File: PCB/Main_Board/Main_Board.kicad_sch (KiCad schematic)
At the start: 34 parts, among them J1 POWER_SUPPLY, J2 LIMIT_SWITCH, J3 ToF, J4 BUCK_IN, J5 BUCK_OUT, J6 ESP32_Left, J7 ESP32_Right, J8 CABLE, J9 MOTOR, U1 74AHCT125

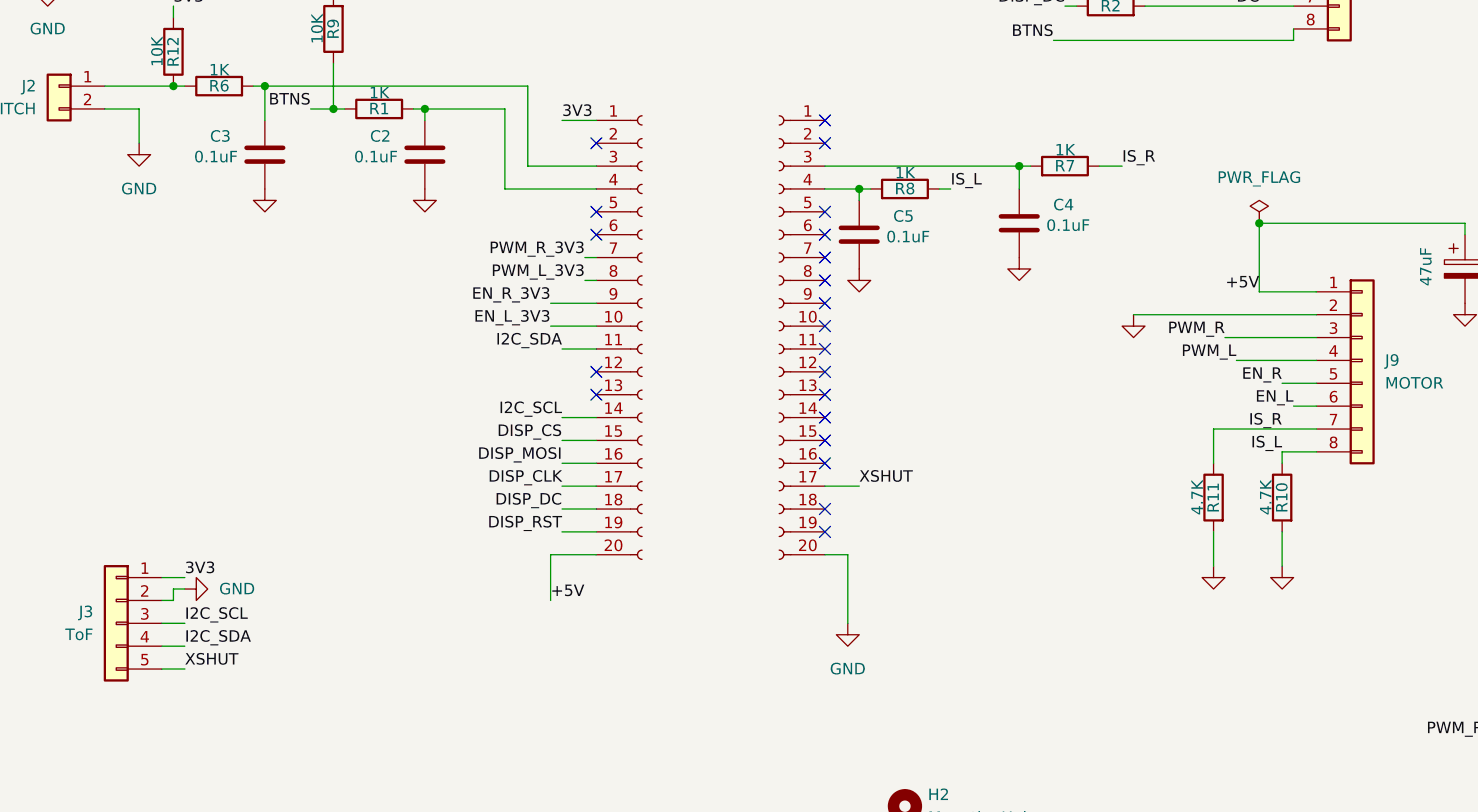
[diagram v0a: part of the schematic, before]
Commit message: Add junctions and wires for improved connectivity on Main Board schematic
- Introduced multiple junctions at specified coordinates to enhance circuit connections.
- Updated wire connections to reflect new junction placements and ensure proper routing.
- Adjusted component positions and labels for clarity and consistency.
- Added two resistors (R13 and R14) with specified values and footprints to the schematic.
- Updated GND symbol and its properties to align with new layout.
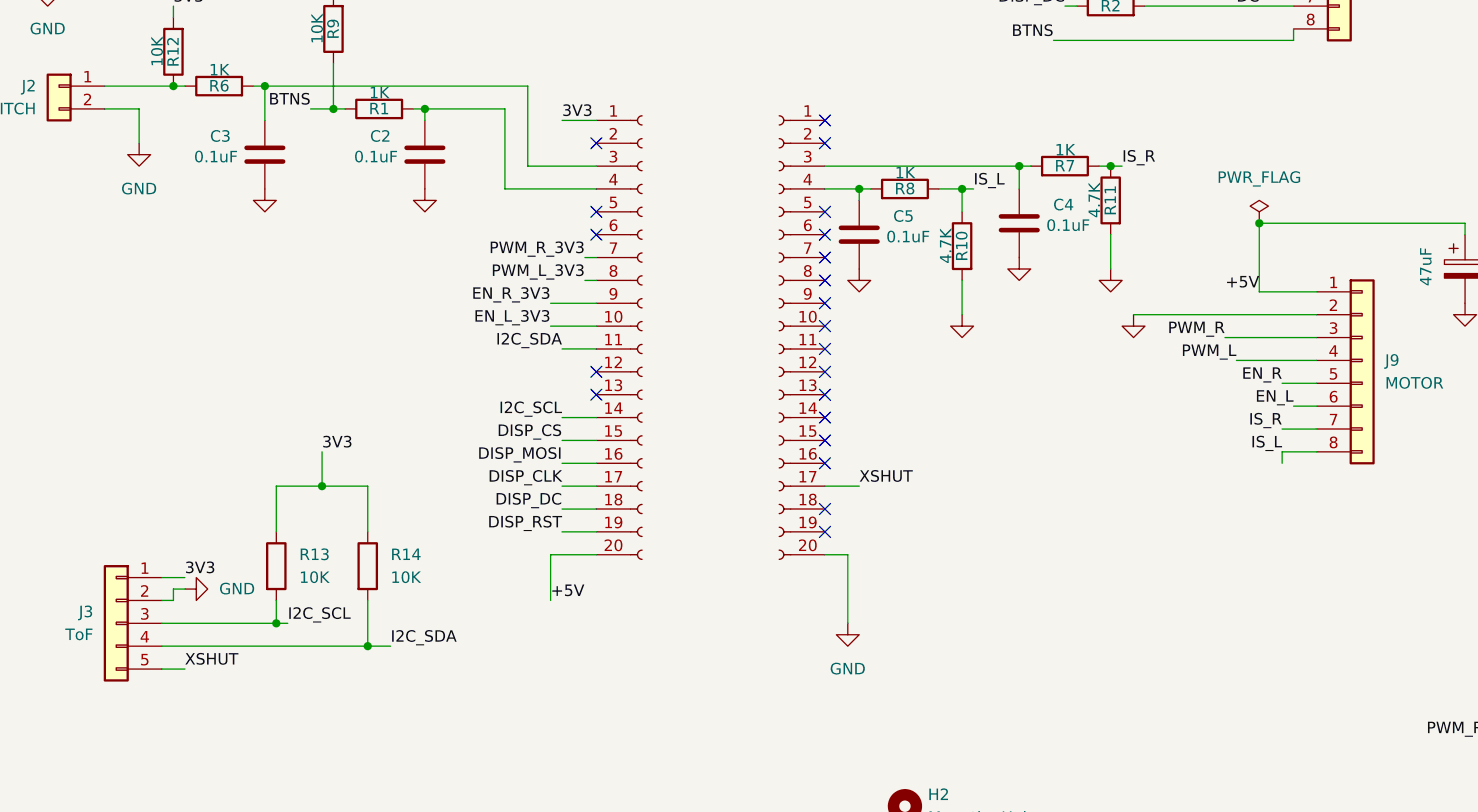
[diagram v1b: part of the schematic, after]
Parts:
- added R13, R14: 10K, Resistor_THT:R_Axial_DIN0207_L6.3mm_D2.5mm_P7.62mm_Horizontal, symbol Device:R
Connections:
- net 3V3: now also R13.1, R14.1
- net I2C_SCL: now also R13.2
- net I2C_SDA: now also R14.2
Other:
- moved on the sheet: R10, R11
